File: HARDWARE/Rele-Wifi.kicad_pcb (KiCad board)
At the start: 2 copper layers, 41 parts, among them J3 Screw_Terminal_01x03, J4 Screw_Terminal_01x03, J5 Screw_Terminal_01x03, J6 Screw_Terminal_01x03, K3 Relay, K4 Relay, K5 Relay, K6 Relay, Q1 2N7002, Q2 2N7002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

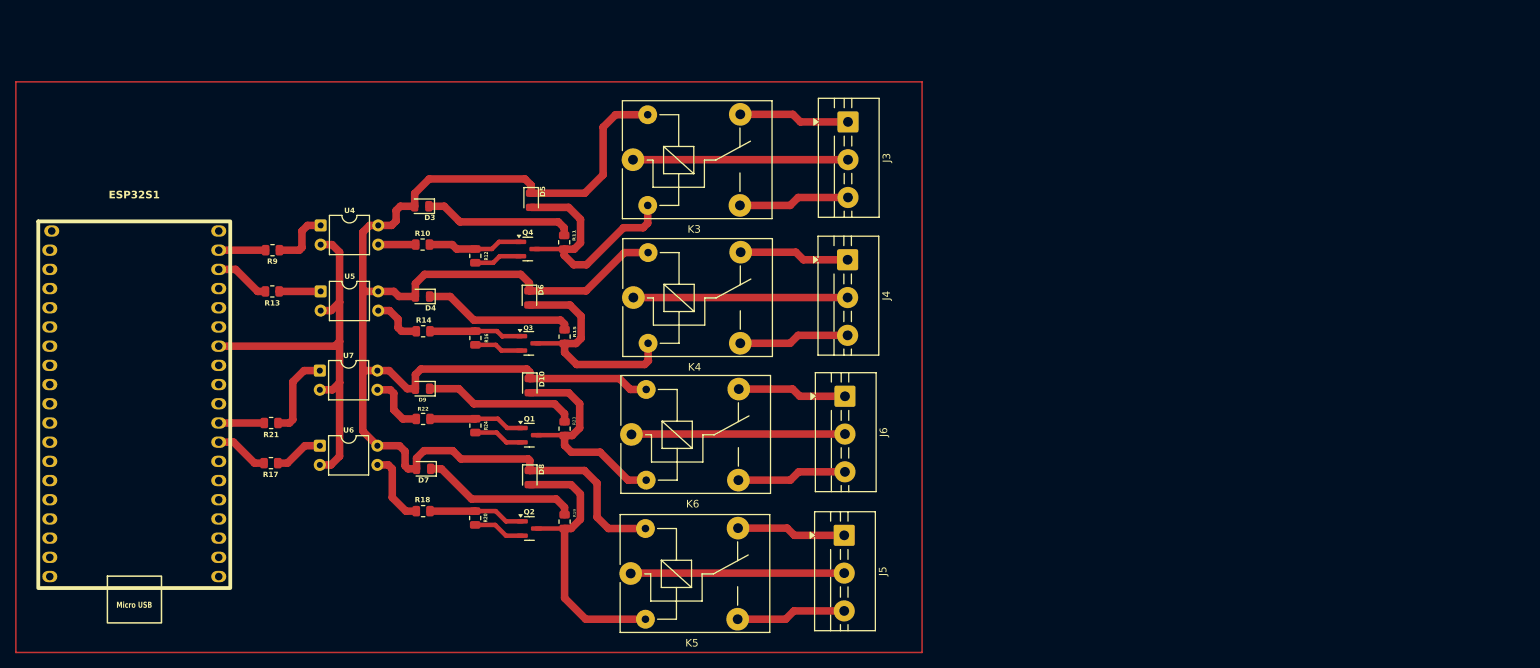
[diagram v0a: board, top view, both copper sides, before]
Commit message: las quintillisas
pcb corregido
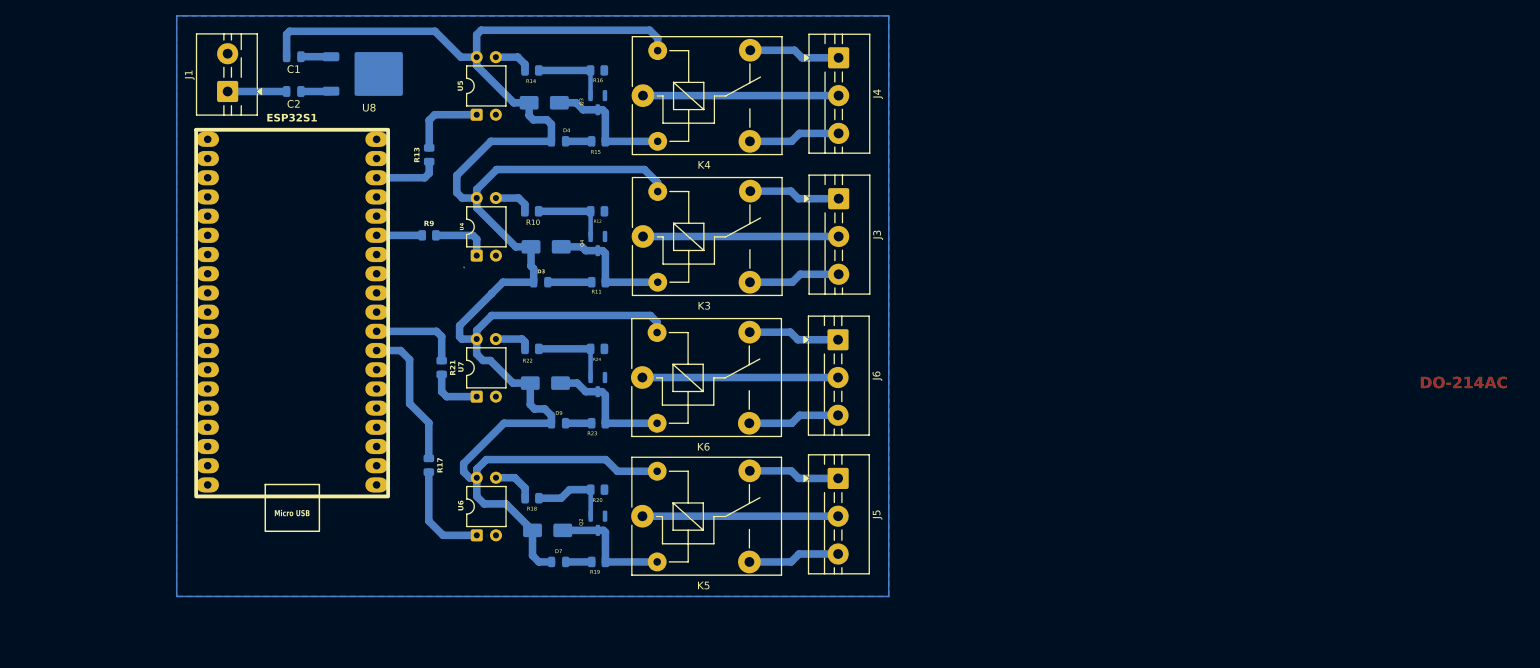
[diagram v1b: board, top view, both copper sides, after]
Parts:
- added C1: C_US, Capacitor_SMD:C_0805_2012Metric, B.Cu at (119.2, 59.3)
- added C2: C, Capacitor_SMD:C_0805_2012Metric, B.Cu at (119.2, 63.9)
- added J1: Screw_Terminal_01x02, TerminalBlock:TerminalBlock_MaiXu_MX126-5.0-02P_1x02_P5.00mm, F.Cu at (110.4, 63.9)
- added U8: KA78M05_TO252, Package_TO_SOT_SMD:TO-252-2, B.Cu at (129.1, 61.6)
- D10, D5, D6, D8: footprint Diode_SMD:D_0805_2012Metric -> Diode_SMD:D_SMA; moved to B.Cu
- D3, D4, D7, D9, Q1, Q2, Q3, Q4, R10, R11, R12, R13, R14, R15, R16, R17, R18, R19, R20, R21, R22, R23, R24, R9: moved to B.Cu
- moved R16 38.9 mm to (159.3, 61.1), turned to 0 degrees
- moved R14 37.4 mm to (150.7, 61.1)
- moved Q3 33.1 mm to (159.4, 65.4), turned to -90 degrees
- moved U5 31.2 mm to (143.4, 67.0), turned to 90 degrees
- moved R13 27.5 mm to (137.1, 72.2), turned to -90 degrees
- moved D4 27.3 mm to (154.2, 70.5)
- moved K4 26.8 mm to (165.4, 64.4)
- moved J4 26.7 mm to (191.3, 59.4)
- moved R15 26.2 mm to (159.5, 70.5), turned to 0 degrees
- moved D6 25.9 mm to (152.3, 65.4), turned to 0 degrees
- moved ESP32S1 24.2 mm to (119.0, 65.4)
- moved U6 23.9 mm to (143.4, 122.6), turned to 90 degrees
- moved R21 23.7 mm to (138.7, 100.4), turned to 90 degrees
- moved D7 21.7 mm to (154.2, 126.1)
- moved U7 21.0 mm to (143.4, 104.2), turned to 90 degrees
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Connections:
- net +5V renamed 5V
- ESP32S1 pad 2: GIO23 -> unconnected-(ESP32S1-GPIO23-Pad2)
- ESP32S1 pad 6: unconnected-(ESP32S1-GPIO21-Pad6) -> GIO21
- Q1 pad 2: <NO NET> -> GND
- Q2 pad 2: <NO NET> -> GND
- Q3 pad 2: <NO NET> -> GND
- Q4 pad 2: <NO NET> -> GND
- R12 pad 2: <NO NET> -> GND
- R16 pad 2: <NO NET> -> GND
- R20 pad 2: <NO NET> -> GND
- R24 pad 2: <NO NET> -> GND
- R9 pad 2: GIO23 -> GIO21
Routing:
- net GND: track 55.2 -> 0.00 mm
- net 5V: track 214.4 -> 261.8 mm
- net <NO NET>: track 26.4 -> 0.00 mm
- net Net-(D8-A): track 37.9 -> 16.5 mm
- net Net-(D7-K): track 20.8 -> 3.43 mm
- net Net-(D9-K): track 20.3 -> 3.43 mm
- net Net-(D5-A): track 33.7 -> 16.9 mm
- net Net-(D4-K): track 20.1 -> 3.43 mm
- net Net-(D6-A): track 32.1 -> 17.4 mm
- net Net-(D3-K): track 20.1 -> 5.79 mm
- net Net-(D10-A): track 30.6 -> 17.3 mm
- net GIO16: track 7.14 -> 18.8 mm
- net Net-(J1-Pin_1): track 0.00 -> 7.80 mm
- net Net-(R17-Pad1): track 6.51 -> 13.6 mm
- net GIO23: track 6.21 -> 0.00 mm
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- added copper zone on B.Cu, net GND
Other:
- board text added: "DO-214AC"
- board text removed: "1KΩ"
- board text removed: "R19"

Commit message: 2,0
pcb terminado
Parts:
- added J2: Conn_01x04, Connector_PinSocket_2.54mm:PinSocket_1x05_P2.54mm_Vertical, F.Cu at (116.5, 69.5)
- added J7: Conn_01x08, Connector_PinSocket_2.54mm:PinSocket_1x08_P2.54mm_Vertical, F.Cu at (124.0, 129.5)
- moved ESP32S1 3.86 mm to (118.5, 69.3)
- moved R9 3.36 mm to (139.1, 85.6)
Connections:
- C1 pad 2: Net-(U8-VO) -> GND
- C2 pad 2: Net-(U8-VI) -> GND
- ESP32S1 pad 20: unconnected-(ESP32S1-3V3-Pad20) -> 3,3V
- ESP32S1 pad 22: unconnected-(ESP32S1-VP-Pad22) -> GIO36
- ESP32S1 pad 23: unconnected-(ESP32S1-VN-Pad23) -> GIO39
- ESP32S1 pad 24: unconnected-(ESP32S1-GPIO34-Pad24) -> GIO34
- ESP32S1 pad 25: unconnected-(ESP32S1-GPIO35-Pad25) -> GIO35
- ESP32S1 pad 26: unconnected-(ESP32S1-GPIO32-Pad26) -> GIO32
- ESP32S1 pad 27: unconnected-(ESP32S1-GPIO33-Pad27) -> GIO33
- ESP32S1 pad 8: unconnected-(ESP32S1-GPIO19-Pad8) -> GIO19
- ESP32S1 pad 9: unconnected-(ESP32S1-GPIO18-Pad9) -> GIO18
- R13 pad 2: GIO22 -> GIO19
- R9 pad 2: GIO21 -> GIO18
- U8 pad 1: Net-(U8-VI) -> Net-(J1-Pin_1)
- U8 pad 3: Net-(U8-VO) -> 5V
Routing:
- net 3,3V: track 0.00 -> 75.3 mm
- net GIO36: track 0.00 -> 61.6 mm
- net GIO39: track 0.00 -> 57.4 mm
- net GIO34: track 0.00 -> 53.5 mm
- net GIO35: track 0.00 -> 49.4 mm
- net GIO32: track 0.00 -> 45.2 mm
- net GIO33: track 0.00 -> 40.8 mm
- net GIO19: track 0.00 -> 23.2 mm
- net GIO18: track 0.00 -> 16.5 mm
- net GIO21: track 6.03 -> 21.7 mm
- net (no net): track 0.10 -> 7.98 mm
- net GIO22: track 8.74 -> 14.0 mm
- net Net-(R9-Pad1): track 7.78 -> 3.38 mm
- net Net-(U8-VI): track 4.00 -> 0.00 mm
- net Net-(U8-VO): track 3.98 -> 0.00 mm
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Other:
- board outline added: 120.5 x 100 mm
- board text removed: "DO-214AC"

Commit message: 3.0
END
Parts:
- U8: footprint Package_TO_SOT_SMD:TO-252-2 -> Package_TO_SOT_SMD:TO-263-3_TabPin2
- moved C2 78.5 mm to (41.5, 75.0), turned to -90 degrees
- moved C1 77.7 mm to (41.5, 59.5), turned to -90 degrees
- moved U8 70.4 mm to (58.8, 65.5)
- moved J3 69.3 mm to (122.3, 84.1)
- moved Q1 69.3 mm to (90.4, 108.7)
- moved Q4 69.3 mm to (90.4, 90.0)
- moved R11 69.3 mm to (90.5, 95.1)
- moved R12 69.3 mm to (90.4, 85.7)
- moved R21 69.3 mm to (69.7, 106.4)
- moved R23 69.3 mm to (90.5, 113.8)
- moved D10 69.3 mm to (83.5, 108.5)
- moved D5 69.3 mm to (83.6, 90.4)
- moved D6 69.3 mm to (83.3, 71.4)
- moved D7 69.3 mm to (85.2, 132.1)
- moved ESP32S1 69.3 mm to (49.5, 75.3)
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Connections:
- ESP32S1 pad 38: unconnected-(ESP32S1-5V-Pad38) -> 5V
- J7 pad 7: 3,3V -> GND
- J7 pad 8: GND -> 5V
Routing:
- net 5V: track 261.8 -> 344.1 mm
- net 3,3V: track 75.3 -> 15.3 mm
- net (no net): track 7.98 -> 0.00 mm
- net Net-(J1-Pin_1): track 7.80 -> 14.8 mm
- net GIO33: track 40.8 -> 39.4 mm
- net GIO35: track 49.4 -> 48.0 mm
- net GIO34: track 53.5 -> 52.1 mm
- net GIO39: track 57.4 -> 56.0 mm
- net GIO36: track 61.6 -> 60.2 mm
- net GIO32: track 45.2 -> 43.8 mm
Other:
- board size 120.5 x 100 mm -> 111.1 x 96.4 mm

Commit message: 4.0
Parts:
- moved D9 2.80 mm to (82.4, 113.8)
- moved D7 2.52 mm to (82.7, 132.1)
- moved D8 1.88 mm to (83.8, 126.1)
- moved R18 1.44 mm to (81.7, 122.3)
- moved U6 1.28 mm to (74.4, 129.9)
- moved D10 1.14 mm to (83.5, 109.6)
- moved R20 0.31 mm to (90.4, 122.3)
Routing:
- net 5V: track 344.1 -> 332.5 mm
- net Net-(D9-K): track 3.43 -> 6.23 mm
- net Net-(D7-K): track 3.43 -> 5.95 mm
- net Net-(R18-Pad1): track 5.76 -> 3.86 mm
- net Net-(D8-A): track 16.5 -> 18.1 mm
- net Net-(R17-Pad1): track 13.6 -> 14.1 mm
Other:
- board size 111.1 x 96.4 mm -> 96.6 x 85.5 mm

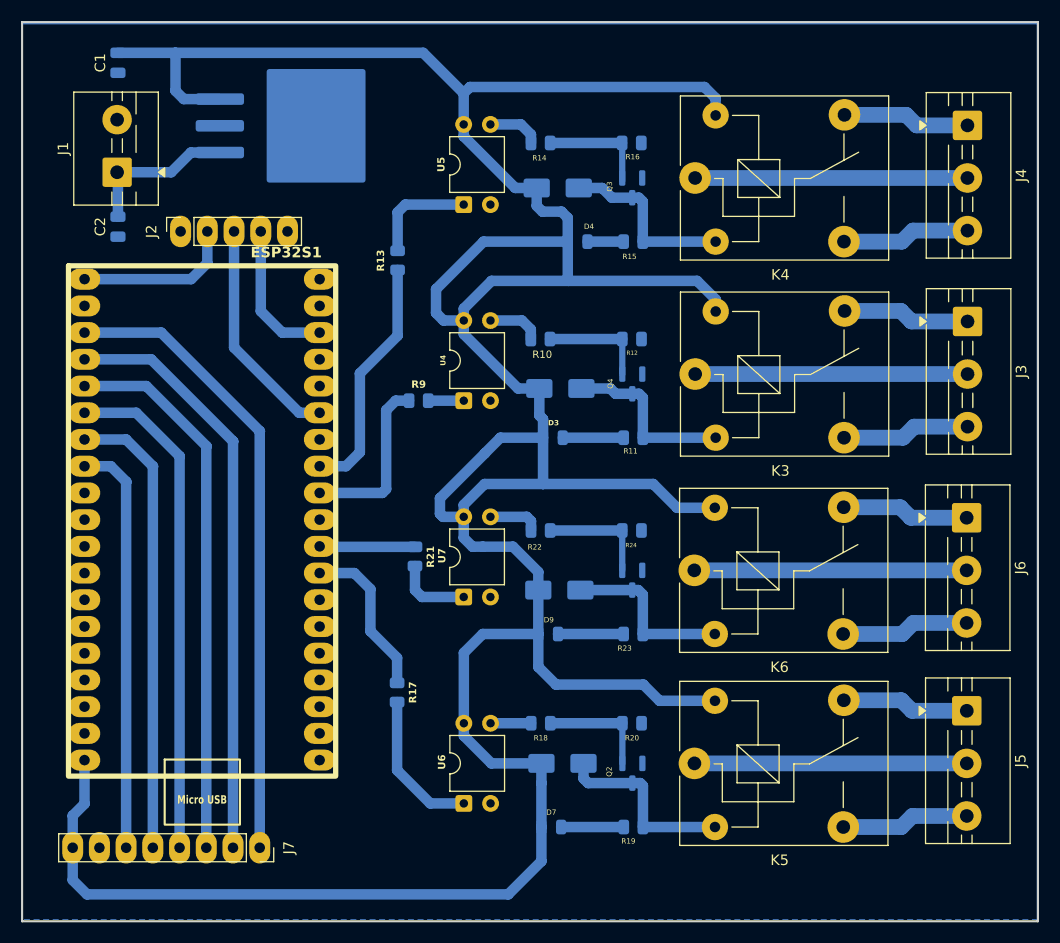
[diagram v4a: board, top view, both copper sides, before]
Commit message: 7805 nueva
EL 7805 SE CAMBIO LA HUELLA
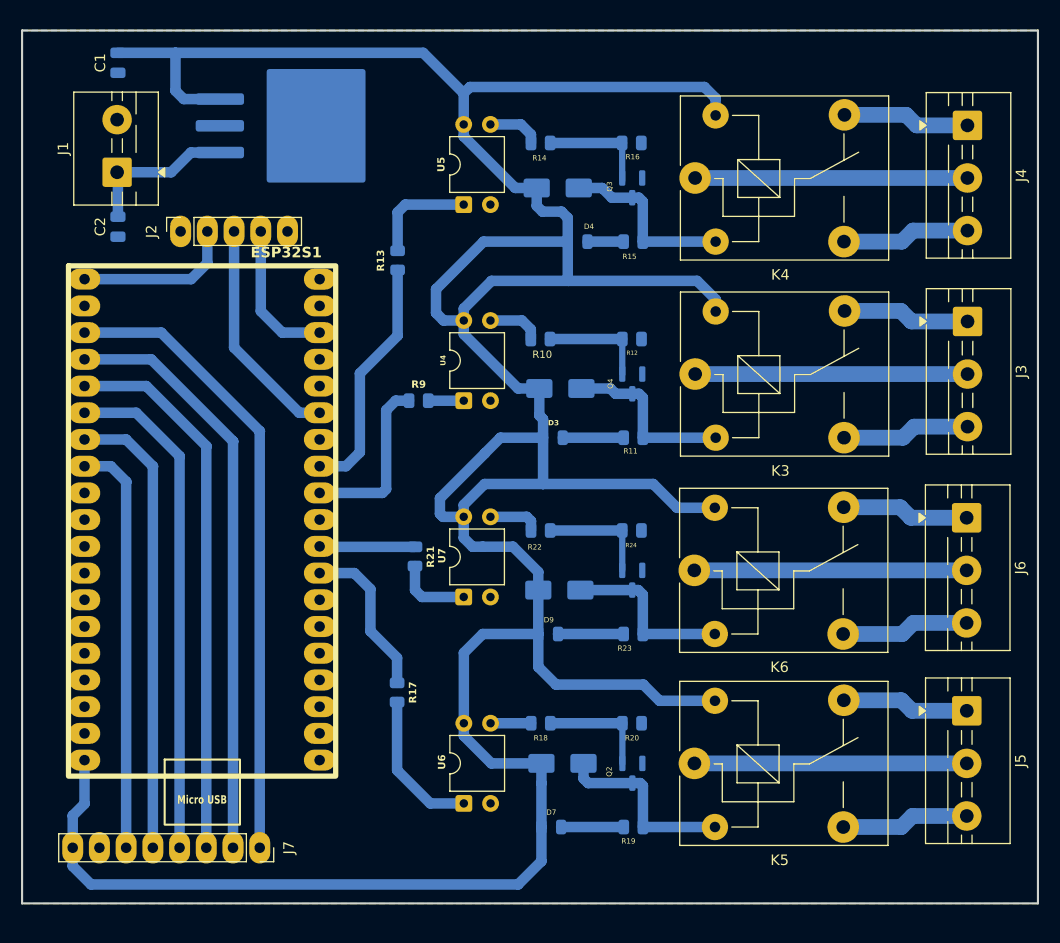
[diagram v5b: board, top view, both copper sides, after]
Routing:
- net 5V: track 332.5 -> 330.9 mm
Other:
- board size 96.6 x 85.5 mm -> 96.6 x 83 mm
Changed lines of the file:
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@@
 	)
 	(gr_rect
-		(start 128.96 55.7)
-		(end 128.96 140.94)
-		(stroke
-			(width 0.2)
-			(type default)
-		)
-		(fill no)
-		(layer "B.Cu")
-	)
-	(gr_rect
-		(start 32.39 55.7)
-		(end 128.96 55.7)
-		(stroke
-			(width 0.2)
-			(type default)
-		)
-		(fill no)
-		(layer "B.Cu")
-	)
-	(gr_rect
-		(start 32.39 55.6)
-		(end 128.96 141.08)
+		(start 32.39 56.4)
+		(end 128.96 139.38)
 		(stroke
 			(width 0.2)
@@
 	)
 	(segment
+		(start 81.76 132.12)
+		(end 81.76 135.37)
+		(width 1)
+		(layer "B.Cu")
+		(net 1)
+	)
+	(segment
 		(start 41.5 58.52)
 		(end 46.97 58.52)
@@
 	)
 	(segment
-		(start 81.76 135.37)
-		(end 81.76 132.12)
-		(width 1)
-		(layer "B.Cu")
-		(net 1)
-	)
-	(segment
 		(start 84.32 80.2)
 		(end 96.5575 80.2)
@@
 	)
 	(segment
-		(start 37.2 134.09)
-		(end 37.2 137.16)
-		(width 1)
-		(layer "B.Cu")
-		(net 1)
-	)
-	(segment
 		(start 74.385 115.565)
 		(end 76.18 113.77)
@@
 	)
 	(segment
+		(start 37.2 135.84)
+		(end 38.94 137.58)
+		(width 1)
+		(layer "B.Cu")
+		(net 1)
+	)
+	(segment
+		(start 81.76 135.37)
+		(end 79.55 137.58)
+		(width 1)
+		(layer "B.Cu")
+		(net 1)
+	)
+	(segment
 		(start 79.54 90.43)
 		(end 74.3775 85.2675)
@@
 	)
 	(segment
+		(start 38.94 137.58)
+		(end 79.55 137.58)
+		(width 1)
+		(layer "B.Cu")
+		(net 1)
+	)
+	(segment
 		(start 37.2 131.04)
 		(end 38.324 129.916)
@@
 	)
 	(segment
-		(start 38.56 138.52)
-		(end 78.61 138.52)
-		(width 1)
-		(layer "B.Cu")
-		(net 1)
-	)
-	(segment
 		(start 92.39 99.51)
 		(end 94.65 101.77)
@@
 	)
 	(segment
-		(start 37.2 137.16)
-		(end 38.56 138.52)
-		(width 1)
-		(layer "B.Cu")
-		(net 1)
-	)
-	(segment
 		(start 76.36113 99.51)
 		(end 81.91 99.51)
@@
 	)
 	(segment
+		(start 37.2 134.09)
+		(end 37.2 135.84)
+		(width 1)
+		(layer "B.Cu")
+		(net 1)
+	)
+	(segment
 		(start 74.37 65.33)
 		(end 74.37 66.46137)
@@
 		(start 71.74 80.99)
 		(end 76.26 76.47)
-		(width 1)
-		(layer "B.Cu")
-		(net 1)
-	)
-	(segment
-		(start 78.61 138.52)
-		(end 81.76 135.37)
 		(width 1)
 		(layer "B.Cu")
@@
 		(layer "B.Cu")
 		(hatch edge 0.5)
-		(connect_pads yes
-			(clearance 1)
+		(connect_pads
+			(clearance 0)
 		)
 		(min_thickness 0.25)
@@
 		(polygon
 			(pts
-				(xy 32.39 55.7) (xy 128.96 55.7) (xy 128.96 140.94) (xy 32.39 140.94)
+				(xy 32.39 56.4) (xy 128.96 56.4) (xy 128.96 139.38) (xy 32.39 139.38)
 			)
 		)

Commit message: CAMBIO DE HUELLA
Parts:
- U8: footprint Package_TO_SOT_SMD:TO-263-3_TabPin2 -> Package_TO_SOT_SMD:TO-263-2
- moved U8 3.74 mm to (62.6, 65.3)
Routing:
- net Net-(J1-Pin_1): track 14.8 -> 18.6 mm
- net 5V: track 330.9 -> 334.3 mm
